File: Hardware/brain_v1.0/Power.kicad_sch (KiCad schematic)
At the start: 46 parts, among them J1 Conn_01x02, J5 Conn_01x02, U1 MP2338GTL-Z, U2 MP2315SGJ-Z, U3 AMS1117-3.3

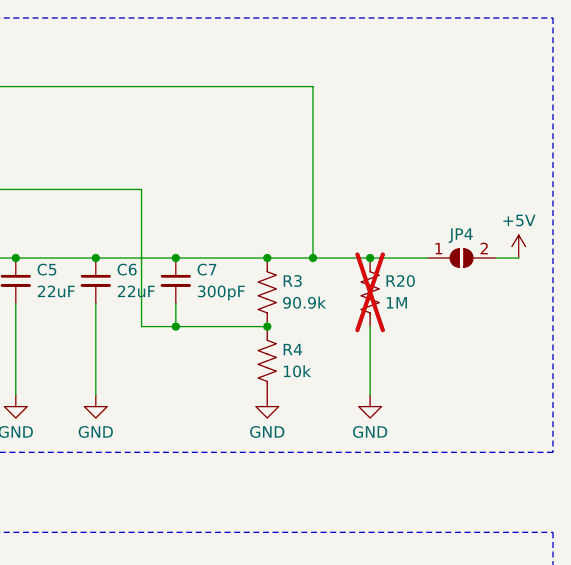
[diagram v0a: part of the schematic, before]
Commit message: brain design pretty much done if RFID not needed
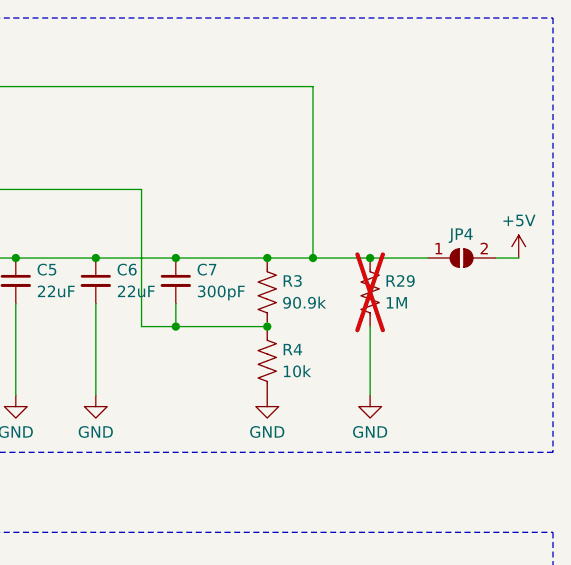
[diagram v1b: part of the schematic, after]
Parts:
- renumbered R20 to R29
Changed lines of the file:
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@@
   (symbol (lib_id "Device:R_US") (at 185.42 49.53 0) (unit 1)
     (in_bom yes) (on_board yes) (dnp yes) (fields_autoplaced)
-    (property "Reference" "R20" (at 187.071 48.3179 0)
+    (property "Reference" "R29" (at 187.071 48.3179 0)
       (effects (font (size 1.27 1.27)) (justify left))
     )

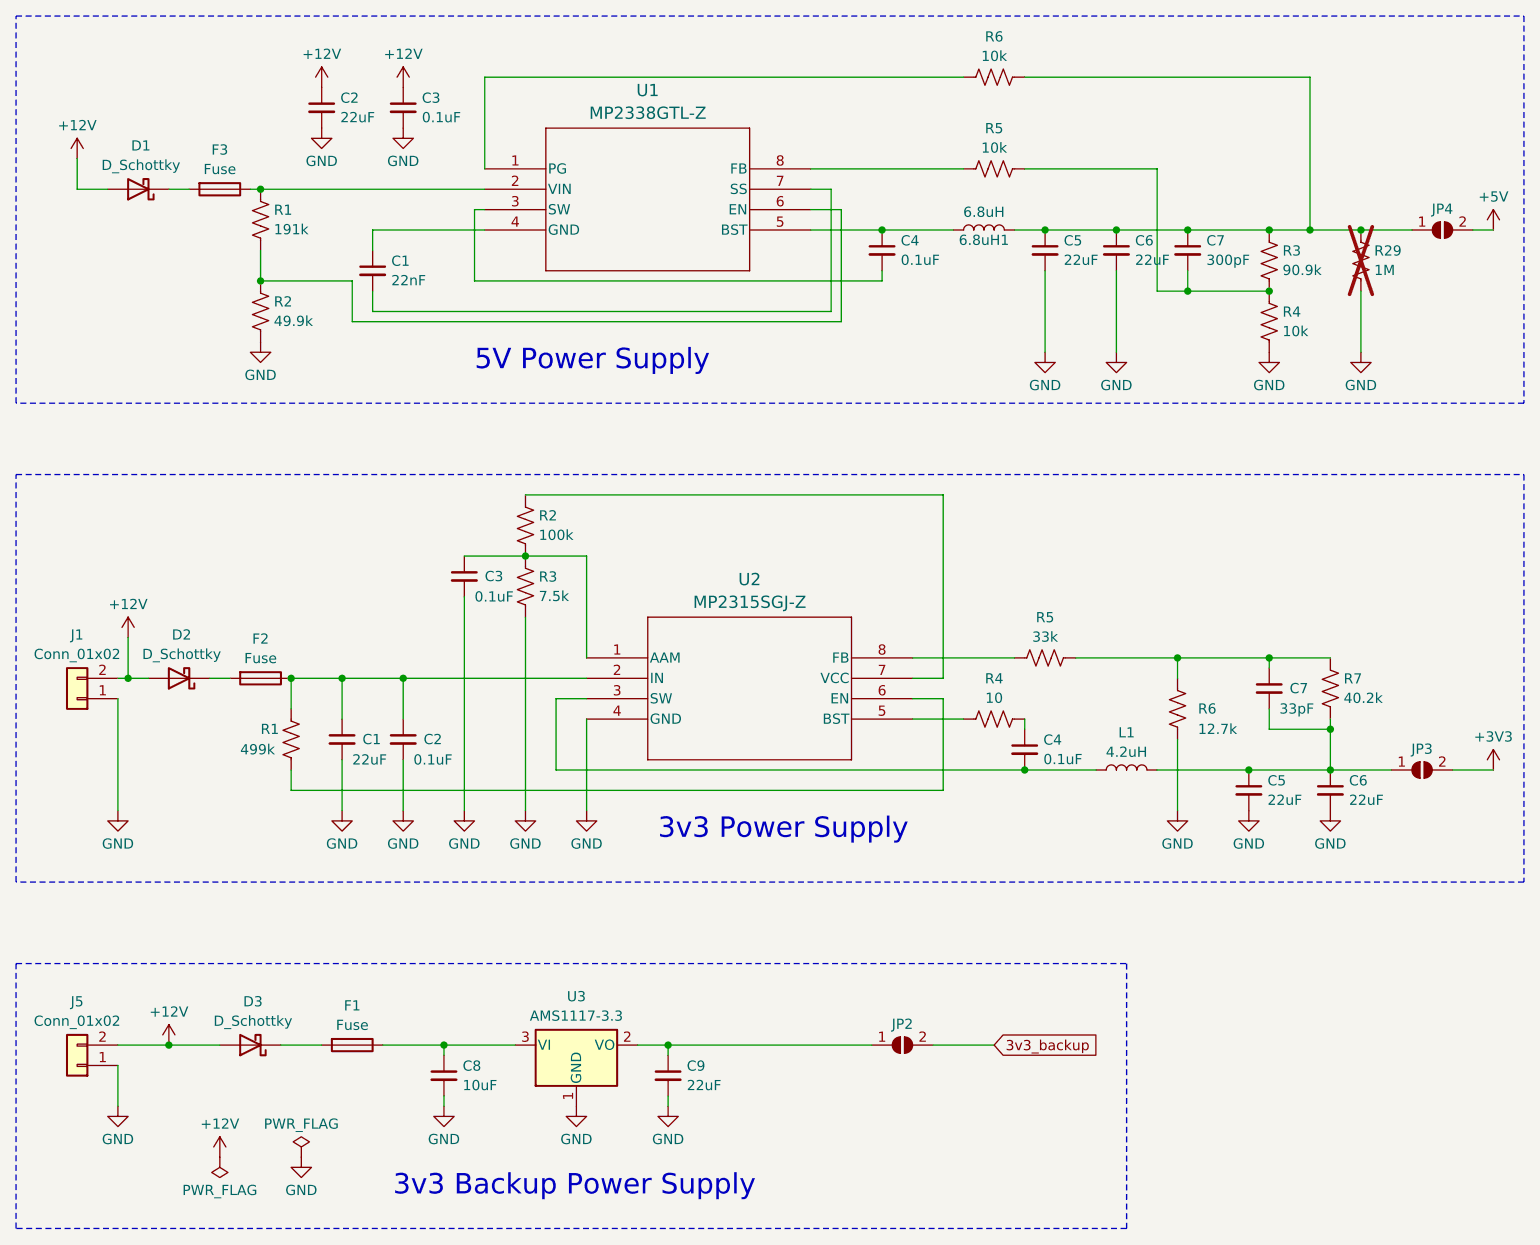
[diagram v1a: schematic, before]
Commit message: finished part selection for power and almost done with part selection for brain--moving to layout next
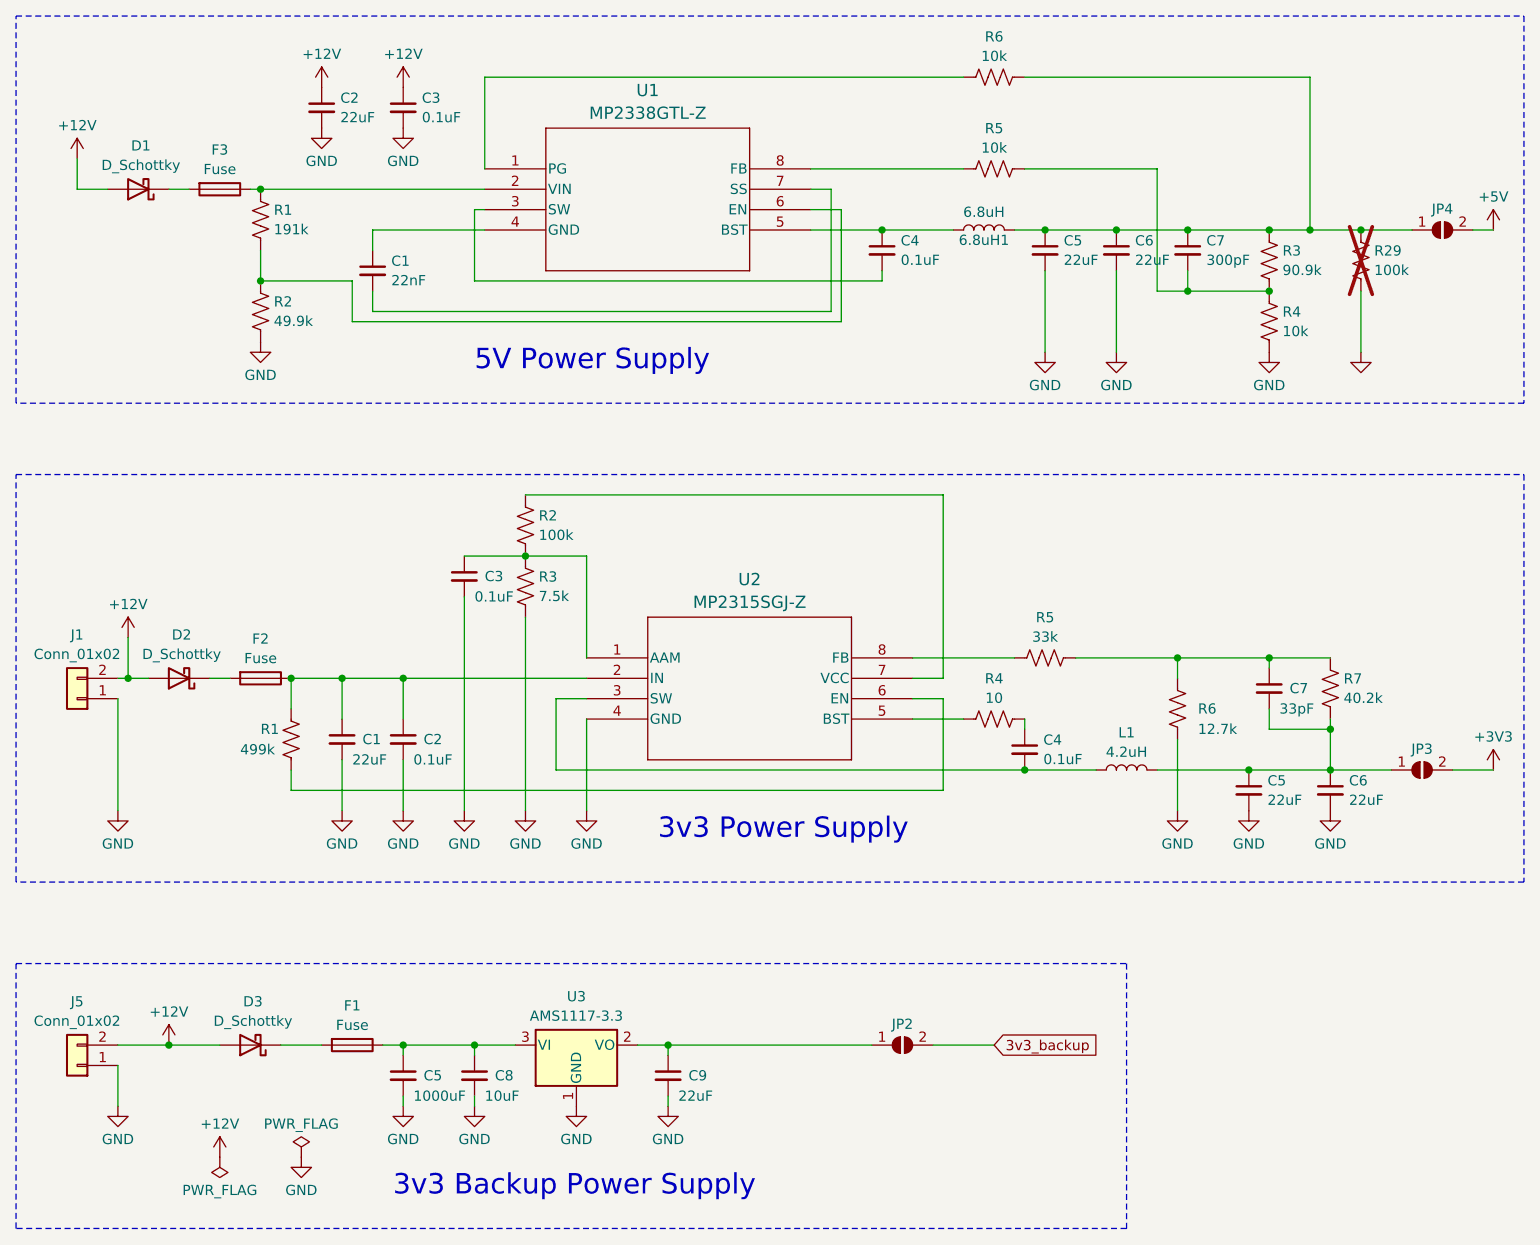
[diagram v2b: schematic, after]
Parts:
- added C5: 1000uF, PCG1A102MCL1GS:CAP_PC_10X12P7_NCH, symbol Device:C_Small
- 6.8uH1: footprint (none) -> 7447786006:WE-PD_6050R; Link (none) -> https://www.digikey.com/en/products/detail/w%C3%BCrth-elekt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; MPN (none) -> 7447786006
- C1: footprint (none) -> Capacitor_SMD:C_0805_2012Metric; Link (none) -> https://www.digikey.com/en/products/detail/kemet/C0805C223F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; MPN (none) -> C0805C223F3GECAUTO
- C1, C2, C5, C6, C9: footprint (none) -> Capacitor_SMD:C_0805_2012Metric; Link (none) -> https://www.digikey.com/en/products/detail/samsung-electro-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; MPN (none) -> CL21A226MAYNNNE
- C2, C3, C4: footprint (none) -> Capacitor_SMD:C_0603_1608Metric; Link (none) -> https://www.digikey.com/en/products/detail/kemet/C0603C103F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; MPN (none) -> C0603C103F3GECAUTO
- C7: footprint (none) -> Resistor_SMD:R_0402_1005Metric; Link (none) -> https://www.digikey.com/en/products/detail/murata-electroni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; MPN (none) -> GJM1555C1H330FB01D
- C7: footprint (none) -> Capacitor_SMD:C_0805_2012Metric; Link (none) -> https://www.digikey.com/en/products/detail/kyocera-avx/0805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; MPN (none) -> 08053C301JAT2A
- C8: footprint (none) -> Resistor_SMD:R_1206_3216Metric; Link (none) -> https://www.digikey.com/en/products/detail/kyocera-avx/F951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; MPN (none) -> F951E106KAAAQ2
- D1, D2, D3: footprint (none) -> VS_30BQ015_M3_9AT:VS_30BQ015_M3_9AT; Link (none) -> https://www.digikey.com/en/products/detail/vishay-general-s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; MPN (none) -> VS-30BQ015-M3/9AT
- F1, F2, F3: footprint (none) -> 4628:FUSE_4628; Link (none) -> https://www.digikey.com/en/products/detail/keystone-electro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; MPN (none) -> 36-4628-ND
- J1, J5: footprint (none) -> Connector_Molex:Molex_KK-254_AE-6410-02A_1x02_P2.54mm_Vertical; Link (none) -> https://www.digikey.com/en/products/detail/molex/1718560102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; MPN (none) -> 1718560102
- JP2, JP3, JP4: footprint (none) -> Jumper:SolderJumper-2_P1.3mm_Open_RoundedPad1.0x1.5mm; Link (none) -> NA; MPN (none) -> NA
- L1: footprint (none) -> 744053004:WE-TPC_5828; Link (none) -> https://www.digikey.com/en/products/detail/w%C3%BCrth-elekt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; MPN (none) -> 744053004
- R1: footprint (none) -> Resistor_SMD:R_1210_3225Metric; Link (none) -> https://www.digikey.com/en/products/detail/panasonic-electr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; MPN (none) -> ERJ-14NF1913U
- R1: footprint (none) -> Resistor_SMD:R_0805_2012Metric; Link (none) -> https://www.digikey.com/en/products/detail/vishay-dale/RCS0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; MPN (none) -> RCS0805499KFKEA
- R2: footprint (none) -> Resistor_SMD:R_0805_2012Metric; Link (none) -> https://www.digikey.com/en/products/detail/yageo/RC0805FR-0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; MPN (none) -> RC0805FR-07100KL
- R2: footprint (none) -> Resistor_SMD:R_2512_6332Metric; Link (none) -> https://www.digikey.com/en/products/detail/stackpole-electr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; MPN (none) -> RMCF2512FT49K9
- R29: value 1M -> 100k; footprint (none) -> Resistor_SMD:R_0805_2012Metric; Link (none) -> https://www.digikey.com/en/products/detail/yageo/RC0805FR-0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; MPN (none) -> RC0805FR-07100KL
- R3: footprint (none) -> Resistor_SMD:R_1206_3216Metric; Link (none) -> https://www.digikey.com/en/products/detail/stackpole-electr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; MPN (none) -> RNCP1206FTD90K9
- R3: footprint (none) -> Resistor_SMD:R_0805_2012Metric; Link (none) -> https://www.digikey.com/en/products/detail/vishay-dale/CRCW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; MPN (none) -> CRCW08057K50FKEAHP
- R4: footprint (none) -> Resistor_SMD:R_2512_6332Metric; Link (none) -> https://www.digikey.com/en/products/detail/te-connectivity-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; MPN (none) -> CRGP2512F10R
- R4, R5, R6: footprint (none) -> Resistor_SMD:R_1206_3216Metric; Link (none) -> https://www.digikey.com/en/products/detail/susumu/HRG3216P-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; MPN (none) -> HRG3216P-1002-B-T1
- R5: footprint (none) -> Resistor_SMD:R_0805_2012Metric; Link (none) -> https://www.digikey.com/en/products/detail/vishay-dale/RCS0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; MPN (none) -> RCS080533K0FKEA
- R6: footprint (none) -> Resistor_SMD:R_1210_3225Metric; Link (none) -> https://www.digikey.com/en/products/detail/vishay-dale/CRCW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; MPN (none) -> CRCW121012K7FKEA
- R7: footprint (none) -> Resistor_SMD:R_0805_2012Metric; Link (none) -> https://www.digikey.com/en/products/detail/vishay-dale/CRCW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; MPN (none) -> CRCW080540K2FKEAHP
- U1: Link (none) -> https://www.digikey.com/en/products/detail/monolithic-power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; MPN (none) -> MP2338GTL-Z
- U2: Link (none) -> https://www.mouser.com/ProductDetail/Monolithic-Power-Syste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; MPN (none) -> MP2315SGJ-Z
- U3: Link (none) -> https://www.digikey.com/en/products/detail/umw/AMS1117-3-3/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; MPN (none) -> AMS1117-3.3
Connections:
- net GND: now also C5.2
- net at C8.1, F1.1, U3.3 (VI): now also C5.1
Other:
- moved on the sheet: C8

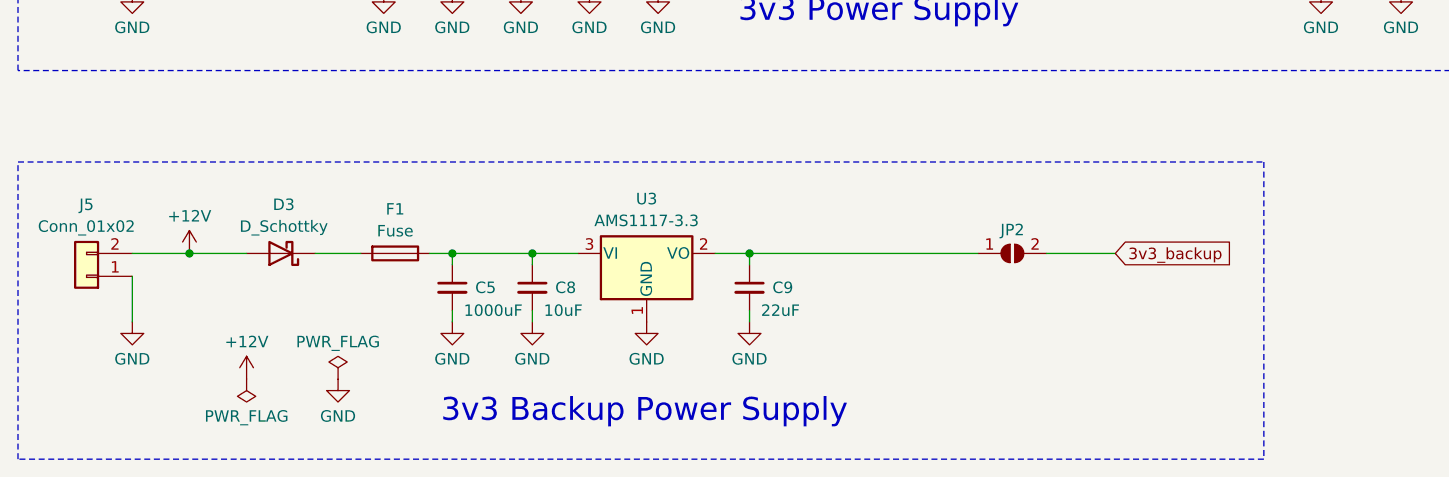
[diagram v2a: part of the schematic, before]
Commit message: everything done on design and parts for first board run except for ADC; onto layout
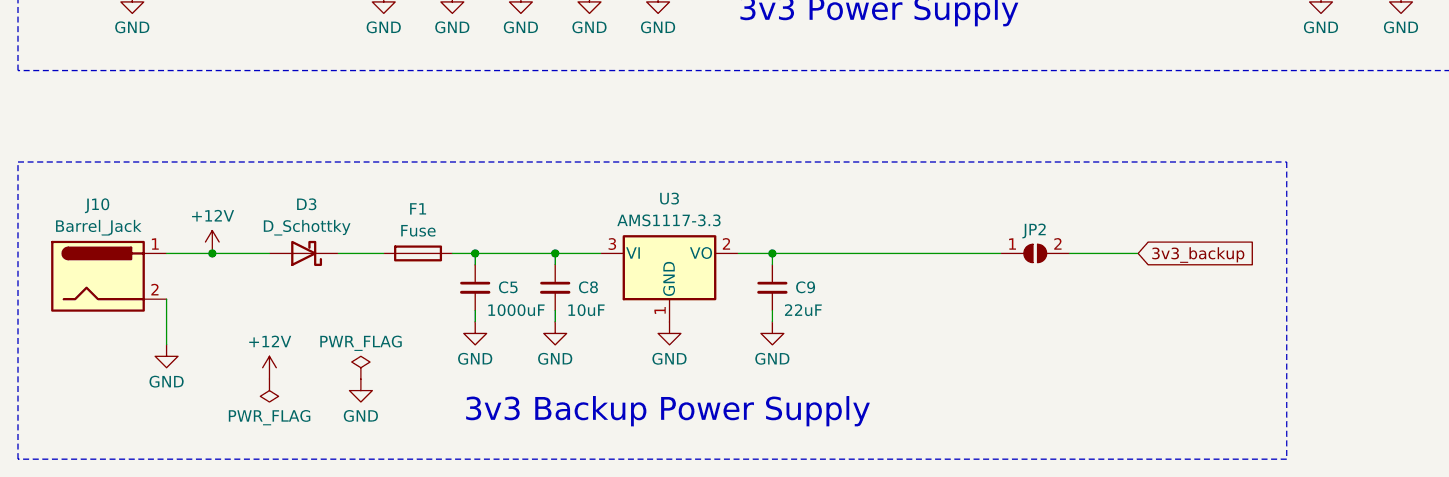
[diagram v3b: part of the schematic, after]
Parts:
- removed J5: Conn_01x02, Connector_Molex:Molex_KK-254_AE-6410-02A_1x02_P2.54mm_Vertical, symbol Connector_Generic:Conn_01x02
- added J10: Barrel_Jack, Connector_BarrelJack:BarrelJack_CUI_PJ-102AH_Horizontal, symbol Connector:Barrel_Jack
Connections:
- net +12V: now also J10.1
- net GND: now also J10.2
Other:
- moved on the sheet: C5, C8, C9, D3, F1, JP2, U3
